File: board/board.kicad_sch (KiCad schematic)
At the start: 25 parts, among them Q1 Q_PMOS_GDS, Q2 Q_NPN_ECB, SW1 SW_Push, SW2 SW_Push, SW3 SW_Push, U1 CC56-12SURKWA

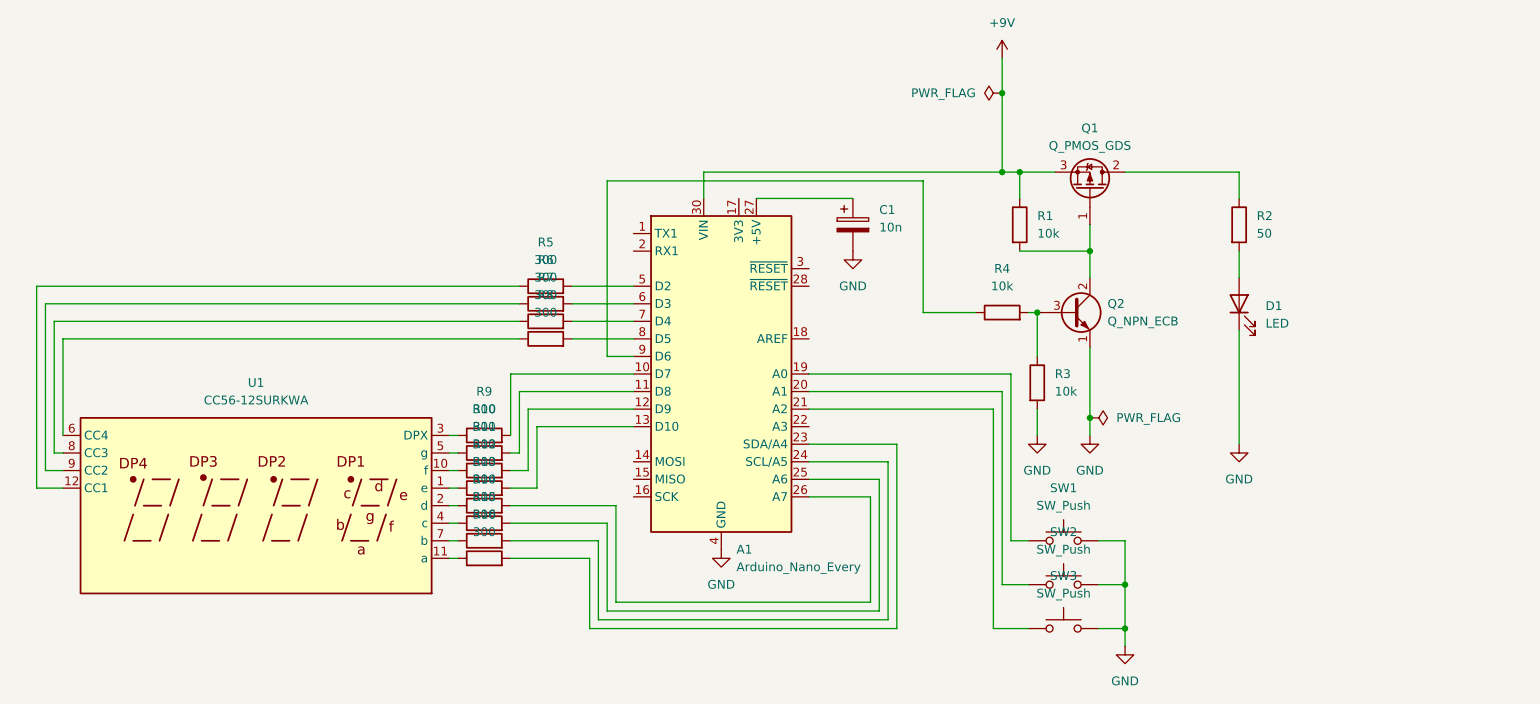
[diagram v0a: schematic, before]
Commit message: implement part of the wiring
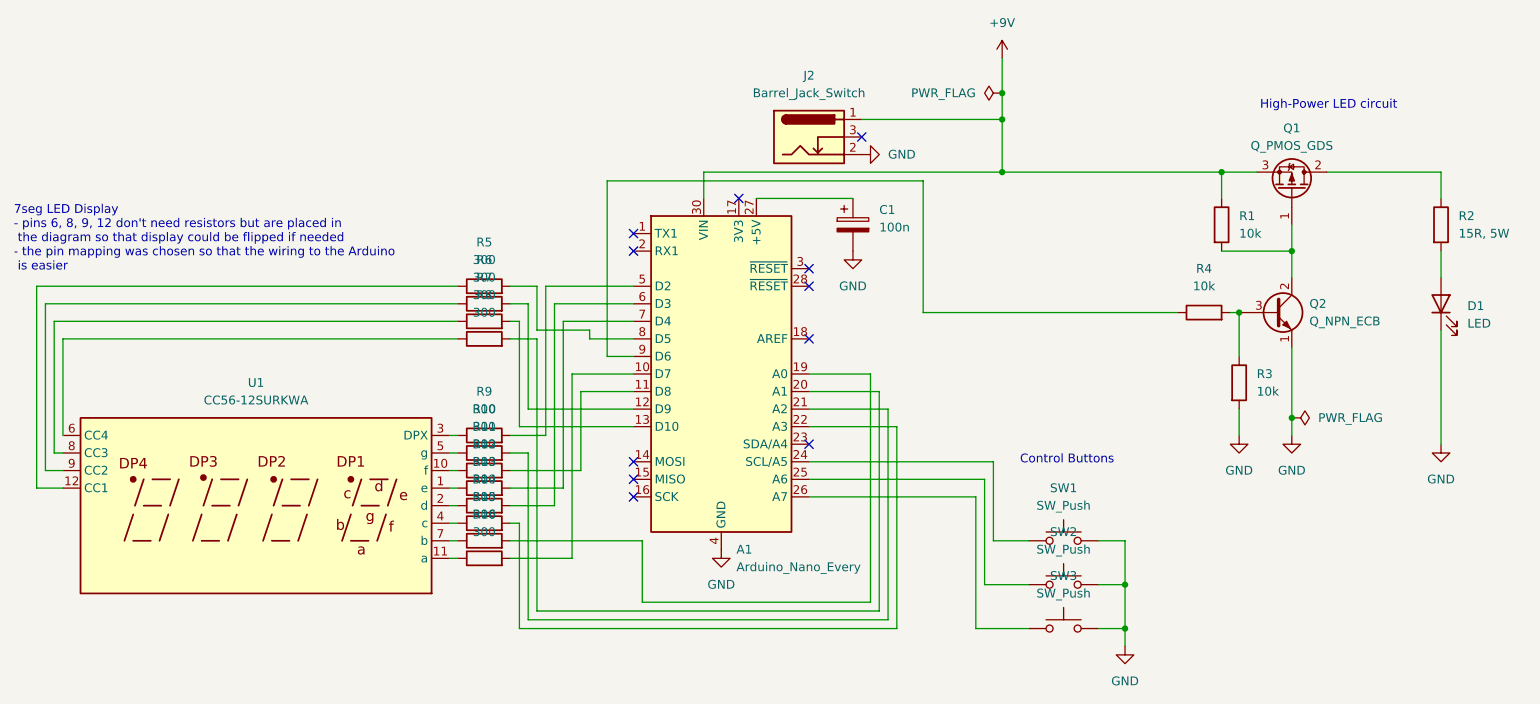
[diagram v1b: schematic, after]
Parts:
- added J2: Barrel_Jack_Switch, Connector_BarrelJack:BarrelJack_Horizontal, symbol Connector:Barrel_Jack_Switch
- C1: value 10n -> 100n; footprint (none) -> Capacitor_THT:C_Disc_D7.0mm_W2.5mm_P5.00mm
- D1: footprint (none) -> Connector_PinHeader_2.54mm:PinHeader_1x02_P2.54mm_Vertical
- Q1: footprint (none) -> Package_TO_SOT_THT:TO-220-3_Horizontal_TabDown
- Q2: footprint (none) -> Package_TO_SOT_THT:TO-92
- R1, R10, R11, R12, R13, R14, R15, R16, R3, R4, R5, R6, R7, R8, R9: footprint (none) -> Resistor_THT:R_Axial_DIN0207_L6.3mm_D2.5mm_P10.16mm_Horizontal
- R2: value 50 -> 15R, 5W; footprint (none) -> Resistor_THT:R_Axial_Power_L20.0mm_W6.4mm_P30.48mm
- SW1, SW2, SW3: footprint (none) -> Button_Switch_THT:SW_PUSH_6mm_H7.3mm
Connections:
- net +9V: now also J2.1
- net GND: now also J2.2
- net at SW1.1: now also A1.24 (SCL/A5); no longer A1.19 (A0)
- net at R13.2: now also A1.6 (D3); no longer A1.26 (A7)
- net at R6.2: now also A1.12 (D9); no longer A1.6 (D3)
- net at R10.2: now also A1.21 (A2); no longer A1.11 (D8)
- net at R15.2: now also A1.19 (A0); no longer A1.24 (SCL/A5)
- net at SW2.1: now also A1.25 (A6); no longer A1.20 (A1)
- net at R7.2: now also A1.13 (D10); no longer A1.7 (D4)
- net at R14.2: now also A1.22 (A3); no longer A1.25 (A6)
- net at R5.2: now also A1.8 (D5); no longer A1.5 (D2)
- net at A1.10 (D7): now also R16.2; no longer R9.2
- net at R11.2: now also A1.11 (D8); no longer A1.12 (D9)
- net at R12.2: now also A1.7 (D4); no longer A1.13 (D10)
- net at SW3.1: now also A1.26 (A7); no longer A1.21 (A2)
- net at A1.23 (SDA/A4): no longer R16.2
- net at R8.2: now also A1.20 (A1); no longer A1.8 (D5)
- new net: A1.5 (D2), R9.2
- no-connect marks 0 -> 11
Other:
- note added: "7seg LED Display - pins 6, 8, 9, 12 don't need resistors but are placed in the diagram so that display could be flipped if needed - the pin mapping was chosen so that the wiring to the Arduino is easier"
- note added: "Control Buttons"
- note added: "High-Power LED circuit"
- company: (none) -> Yasu
- title: (none) -> Artificial Sun
- moved on the sheet: D1, Q1, Q2, R1, R2, R3, R4, R5, R6, R7, R8

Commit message: more compact board
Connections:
- net at A1.5 (D2): now also R12.2; no longer R9.2
- net at A1.7 (D4): now also R9.2; no longer R12.2
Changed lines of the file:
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@@
+	(wire
+		(pts
+			(xy 100.33 59.69) (xy 105.41 59.69)
+		)
+		(stroke
+			(width 0)
+			(type default)
+		)
+	)
 	(wire
 		(pts
@@
 	(wire
 		(pts
-			(xy 92.71 81.28) (xy 92.71 59.69)
-		)
-		(stroke
-			(width 0)
-			(type default)
-		)
-	)
-	(wire
-		(pts
 			(xy 200.66 68.58) (xy 200.66 78.74)
 		)
@@
 	(wire
 		(pts
-			(xy 95.25 88.9) (xy 87.63 88.9)
-		)
-		(stroke
-			(width 0)
-			(type default)
-		)
-	)
-	(wire
-		(pts
 			(xy 143.51 109.22) (xy 143.51 80.01)
 		)
@@
 	(wire
 		(pts
+			(xy 100.33 88.9) (xy 100.33 59.69)
+		)
+		(stroke
+			(width 0)
+			(type default)
+		)
+	)
+	(wire
+		(pts
+			(xy 87.63 88.9) (xy 100.33 88.9)
+		)
+		(stroke
+			(width 0)
+			(type default)
+		)
+	)
+	(wire
+		(pts
+			(xy 102.87 64.77) (xy 105.41 64.77)
+		)
+		(stroke
+			(width 0)
+			(type default)
+		)
+	)
+	(wire
+		(pts
 			(xy 172.72 109.22) (xy 176.53 109.22)
 		)
@@
 	(wire
 		(pts
+			(xy 102.87 81.28) (xy 102.87 64.77)
+		)
+		(stroke
+			(width 0)
+			(type default)
+		)
+	)
+	(wire
+		(pts
 			(xy 176.53 102.87) (xy 176.53 109.22)
 		)
@@
 	(wire
 		(pts
+			(xy 87.63 81.28) (xy 102.87 81.28)
+		)
+		(stroke
+			(width 0)
+			(type default)
+		)
+	)
+	(wire
+		(pts
 			(xy 90.17 62.23) (xy 90.17 77.47)
 		)
@@
 	(wire
 		(pts
-			(xy 87.63 81.28) (xy 92.71 81.28)
-		)
-		(stroke
-			(width 0)
-			(type default)
-		)
-	)
-	(wire
-		(pts
 			(xy 222.25 66.04) (xy 222.25 82.55)
 		)
@@
 	(wire
 		(pts
-			(xy 92.71 59.69) (xy 105.41 59.69)
-		)
-		(stroke
-			(width 0)
-			(type default)
-		)
-	)
-	(wire
-		(pts
 			(xy 87.63 96.52) (xy 106.68 96.52)
 		)
@@
 	(wire
 		(pts
-			(xy 95.25 64.77) (xy 95.25 88.9)
-		)
-		(stroke
-			(width 0)
-			(type default)
-		)
-	)
-	(wire
-		(pts
 			(xy 191.77 63.5) (xy 193.04 63.5)
 		)
@@
 		)
 		(stroke
-			(width 0)
-			(type default)
-		)
-	)
-	(wire
-		(pts
-			(xy 105.41 64.77) (xy 95.25 64.77)
-		)
-		(stroke
